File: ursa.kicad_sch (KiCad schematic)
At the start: 36 parts, among them SW10_L1 SW_Push, SW10_R1 SW_Push, SW11_L1 SW_Push, SW11_R1 SW_Push, SW12_L1 SW_Push, SW12_R1 SW_Push, SW13_L1 SW_Push, SW13_R1 SW_Push, SW14_L1 SW_Push, SW14_R1 SW_Push, SW15_L1 SW_Push, SW15_R1 SW_Push, SW16_L1 SW_Push, SW16_R1 SW_Push, SW17_L1 SW_Push, SW17_R1 SW_Push, SW1_L1 SW_Push, SW1_R1 SW_Push, SW2_L1 SW_Push, SW2_R1 SW_Push, SW3_L1 SW_Push, SW3_R1 SW_Push, SW4_L1 SW_Push, SW4_R1 SW_Push, SW5_L1 SW_Push, SW5_R1 SW_Push, SW6_L1 SW_Push, SW6_R1 SW_Push, SW7_L1 SW_Push, SW7_R1 SW_Push, SW8_L1 SW_Push, SW8_R1 SW_Push, SW9_L1 SW_Push, SW9_R1 SW_Push, U1_L1 WeAct-RP2040-Pico, U1_R1 WeAct-RP2040-Pico

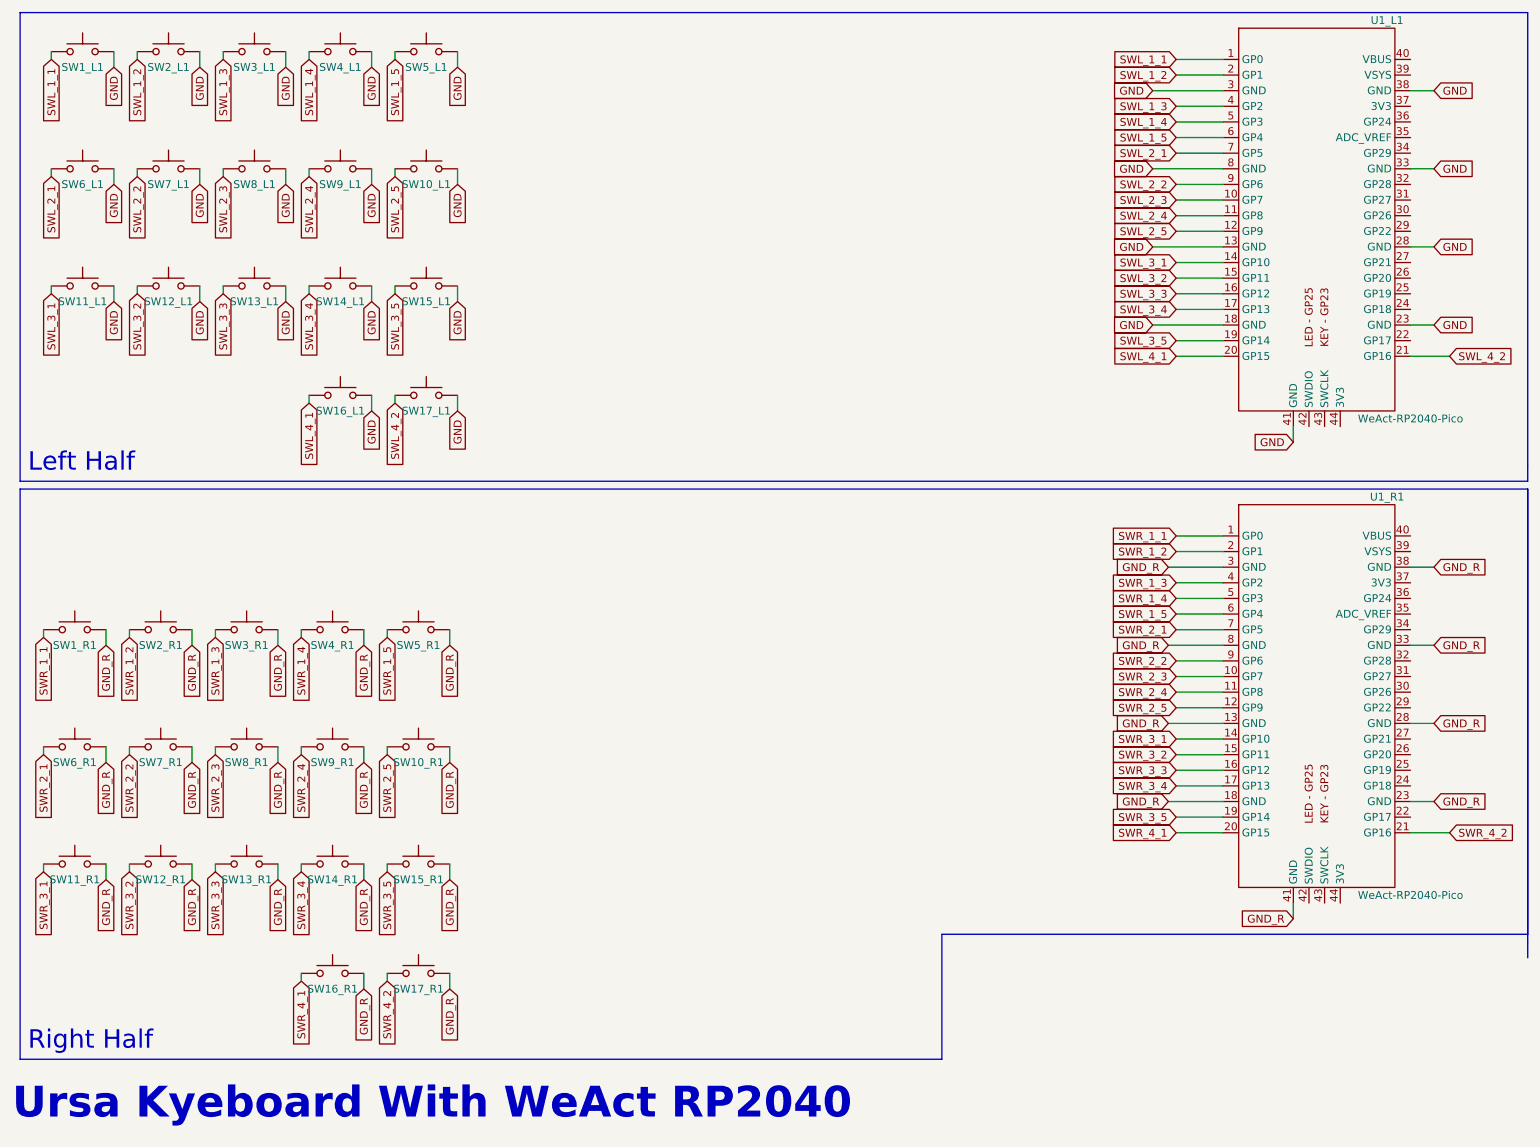
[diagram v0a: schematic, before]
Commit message: better wiring and through hole added
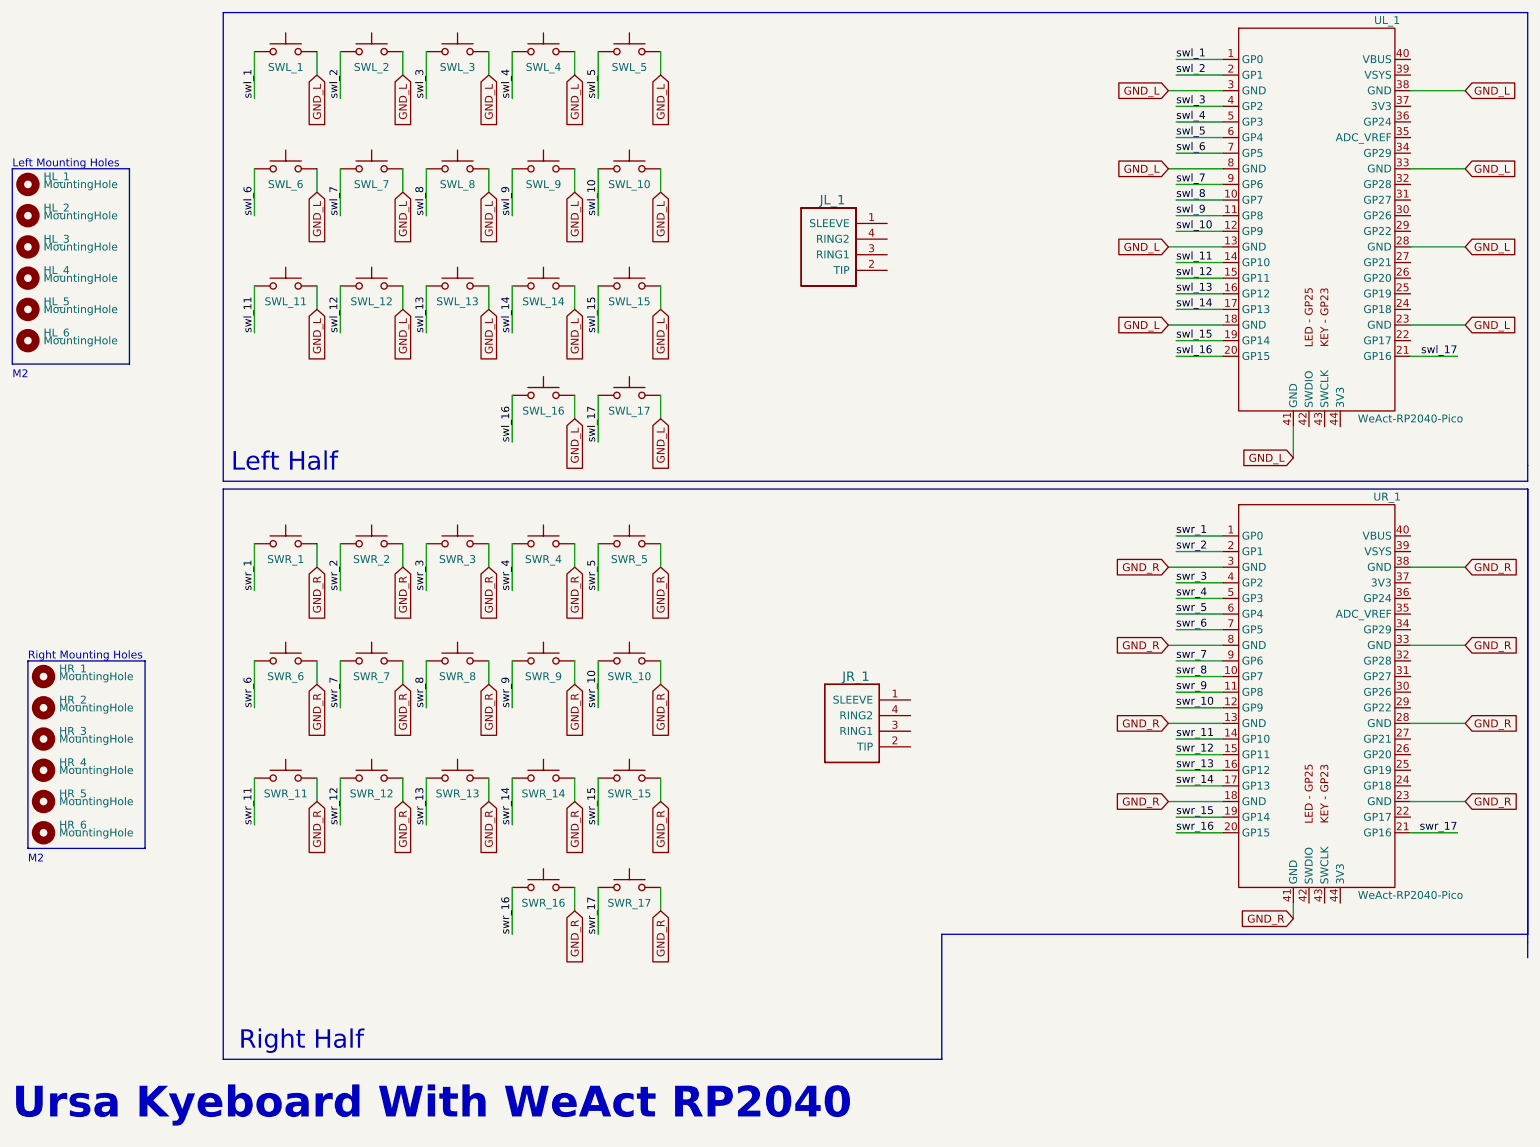
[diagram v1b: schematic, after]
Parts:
- removed U1_L1, U1_R1: WeAct-RP2040-Pico, WeAct-RP2040-Pico:WeAct-RP2040-Pico, symbol WeAct-RP2040-Pico:WeAct-RP2040-Pico
- added HL_1, HL_2, HL_3, HL_4, HL_5, HL_6, HR_1, HR_2, HR_3, HR_4, HR_5, HR_6: MountingHole, MountingHole:MountingHole_2.2mm_M2, symbol Mechanical:MountingHole
- added JL_1, JR_1: TRRS, Keebio:TRRS-PJ-320A, symbol TRRS:TRRS
- added UL_1, UR_1: WeAct-RP2040-Pico, WeAct-RP2040-Pico:WeAct-RP2040-Pico, symbol WeAct-RP2040-Pico:WeAct-RP2040-Pico
- renumbered SW1_L1 to SWL_1, SW10_L1 to SWL_10, SW11_L1 to SWL_11, SW12_L1 to SWL_12, SW13_L1 to SWL_13, SW14_L1 to SWL_14, SW15_L1 to SWL_15, SW16_L1 to SWL_16, SW17_L1 to SWL_17, SW2_L1 to SWL_2, SW3_L1 to SWL_3, SW4_L1 to SWL_4, SW5_L1 to SWL_5, SW6_L1 to SWL_6, SW7_L1 to SWL_7, SW8_L1 to SWL_8, SW9_L1 to SWL_9, SW1_R1 to SWR_1, SW10_R1 to SWR_10, SW11_R1 to SWR_11, SW12_R1 to SWR_12, SW13_R1 to SWR_13, SW14_R1 to SWR_14, SW15_R1 to SWR_15, SW16_R1 to SWR_16, SW17_R1 to SWR_17, SW2_R1 to SWR_2, SW3_R1 to SWR_3, SW4_R1 to SWR_4, SW5_R1 to SWR_5, SW6_R1 to SWR_6, SW7_R1 to SWR_7, SW8_R1 to SWR_8, SW9_R1 to SWR_9
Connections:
- net GND_R: now also UR_1.13 (GND), UR_1.18 (GND), UR_1.23 (GND), UR_1.28 (GND), UR_1.3 (GND), UR_1.33 (GND), UR_1.38 (GND), UR_1.41 (GND), UR_1.8 (GND)
- net GND renamed GND_L
- net GND_L: now also UL_1.13 (GND), UL_1.18 (GND), UL_1.23 (GND), UL_1.28 (GND), UL_1.3 (GND), UL_1.33 (GND), UL_1.38 (GND), UL_1.41 (GND), UL_1.8 (GND)
- net SWL_1_1 renamed swl_1
- net swl_1: now also UL_1.1 (GP0)
- net SWL_1_2 renamed swl_2
- net swl_2: now also UL_1.2 (GP1)
- net SWL_1_3 renamed swl_3
- net swl_3: now also UL_1.4 (GP2)
- net SWL_1_4 renamed swl_4
- net swl_4: now also UL_1.5 (GP3)
- net SWL_1_5 renamed swl_5
- net swl_5: now also UL_1.6 (GP4)
- net SWL_2_1 renamed swl_6
- net swl_6: now also UL_1.7 (GP5)
- net SWL_2_2 renamed swl_7
- net swl_7: now also UL_1.9 (GP6)
- net SWL_2_3 renamed swl_8
- net swl_8: now also UL_1.10 (GP7)
- net SWL_2_4 renamed swl_9
- net swl_9: now also UL_1.11 (GP8)
- net SWL_2_5 renamed swl_10
- net swl_10: now also UL_1.12 (GP9)
- net SWL_3_1 renamed swl_11
- net swl_11: now also UL_1.14 (GP10)
- net SWL_3_2 renamed swl_12
- net swl_12: now also UL_1.15 (GP11)
- net SWL_3_3 renamed swl_13
- net swl_13: now also UL_1.16 (GP12)
- net SWL_3_4 renamed swl_14
- net swl_14: now also UL_1.17 (GP13)
- net SWL_3_5 renamed swl_15
- net swl_15: now also UL_1.19 (GP14)
- net SWL_4_1 renamed swl_16
- net swl_16: now also UL_1.20 (GP15)
- net SWL_4_2 renamed swl_17
- net swl_17: now also UL_1.21 (GP16)
- net SWR_1_1 renamed swr_1
- net swr_1: now also UR_1.1 (GP0)
- net SWR_1_2 renamed swr_2
- net swr_2: now also UR_1.2 (GP1)
- net SWR_1_3 renamed swr_3
- net swr_3: now also UR_1.4 (GP2)
- net SWR_1_4 renamed swr_4
- net swr_4: now also UR_1.5 (GP3)
- net SWR_1_5 renamed swr_5
- net swr_5: now also UR_1.6 (GP4)
- net SWR_2_1 renamed swr_6
- net swr_6: now also UR_1.7 (GP5)
- net SWR_2_2 renamed swr_7
- net swr_7: now also UR_1.9 (GP6)
- net SWR_2_3 renamed swr_8
- net swr_8: now also UR_1.10 (GP7)
- net SWR_2_4 renamed swr_9
- net swr_9: now also UR_1.11 (GP8)
- net SWR_2_5 renamed swr_10
- net swr_10: now also UR_1.12 (GP9)
- net SWR_3_1 renamed swr_11
- net swr_11: now also UR_1.14 (GP10)
- net SWR_3_2 renamed swr_12
- net swr_12: now also UR_1.15 (GP11)
- net SWR_3_3 renamed swr_13
- net swr_13: now also UR_1.16 (GP12)
- net SWR_3_4 renamed swr_14
- net swr_14: now also UR_1.17 (GP13)
- net SWR_3_5 renamed swr_15
- net swr_15: now also UR_1.19 (GP14)
- net SWR_4_1 renamed swr_16
- net swr_16: now also UR_1.20 (GP15)
- net SWR_4_2 renamed swr_17
- net swr_17: now also UR_1.21 (GP16)
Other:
- note added: "Left Mounting Holes"
- note added: "M2"
- note added: "Right Mounting Holes"
- moved on the sheet: SWL_1, SWL_10, SWL_11, SWL_12, SWL_13, SWL_14, SWL_15, SWL_16, SWL_17, SWL_2, SWL_3, SWL_4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
